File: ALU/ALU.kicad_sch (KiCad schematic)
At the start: 1 part

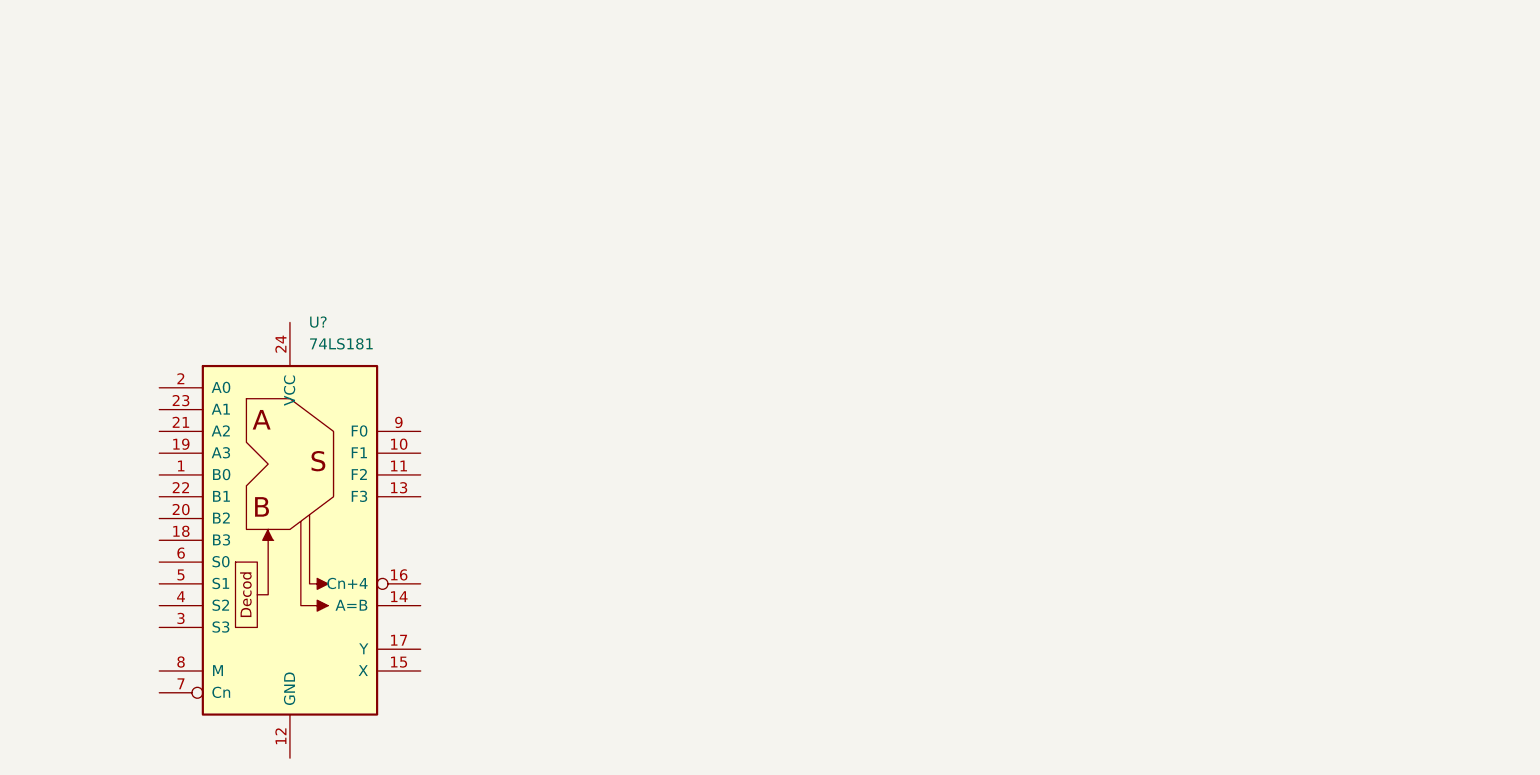
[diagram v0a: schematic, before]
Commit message: Completed ALU first draft
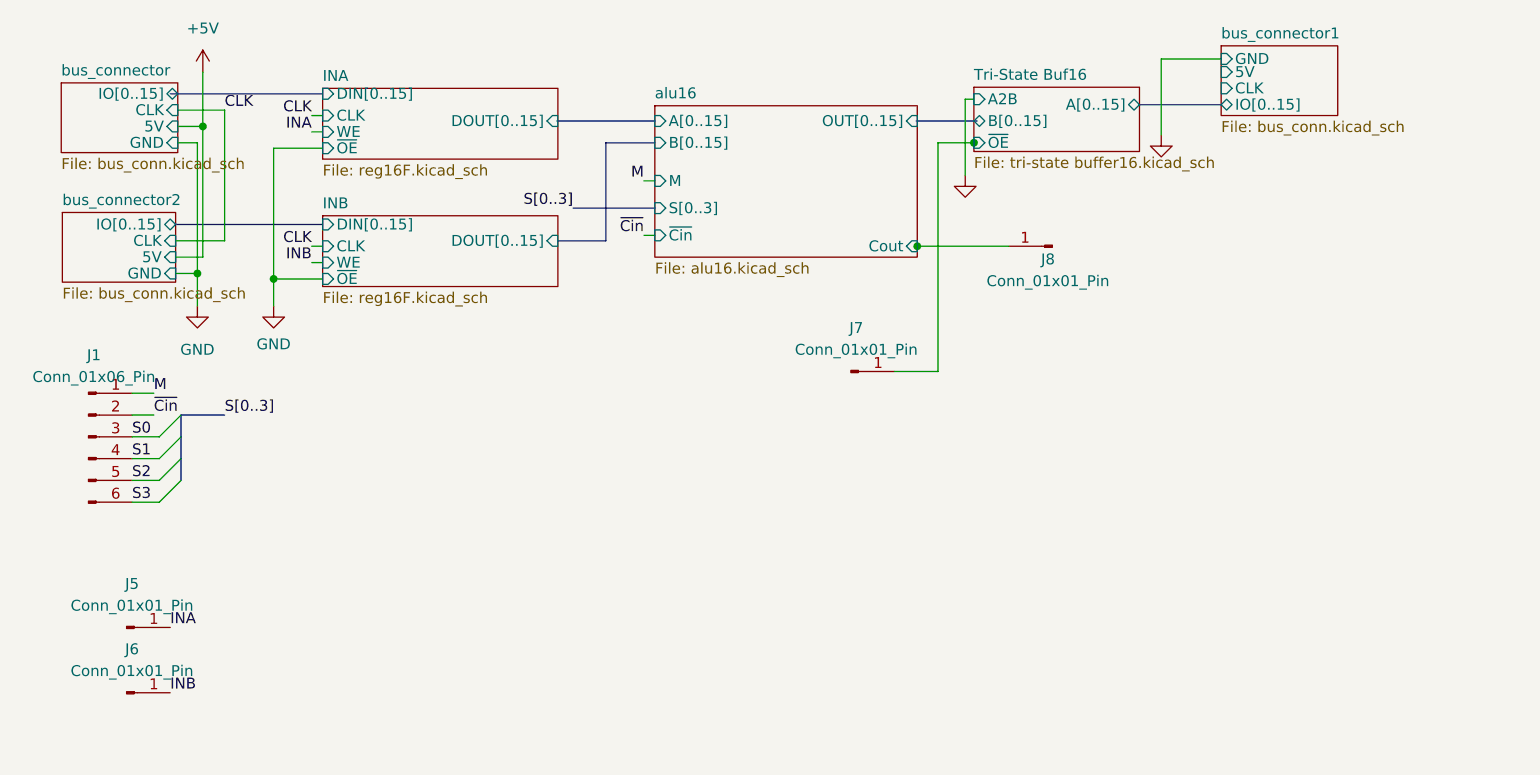
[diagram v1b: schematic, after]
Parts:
- removed U?: 74LS181, symbol 74xx:74LS181
- added J1: Conn_01x06_Pin, Connector_PinHeader_2.54mm:PinHeader_1x06_P2.54mm_Vertical, symbol Connector:Conn_01x06_Pin
- added J5, J6, J7, J8: Conn_01x01_Pin, Connector_PinHeader_2.54mm:PinHeader_1x01_P2.54mm_Vertical, symbol Connector:Conn_01x01_Pin
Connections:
- new net INA: J5.1 (Pin_1)
- new net INB: J6.1 (Pin_1)
- new net M: J1.1 (Pin_1)
- new net S0: J1.3 (Pin_3)
- new net S1: J1.4 (Pin_4)
- new net S2: J1.5 (Pin_5)
- new net S3: J1.6 (Pin_6)
- new net Tri-State Buf16/~{OE}: J7.1 (Pin_1)
- new net alu16/Cout: J8.1 (Pin_1)
- new net ~{Cin}: J1.2 (Pin_2)
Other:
- added sheet INA (reg16F.kicad_sch)
- added sheet INB (reg16F.kicad_sch)
- added sheet Tri-State Buf16 (tri-state buffer16.kicad_sch)
- added sheet alu16 (alu16.kicad_sch)
- added sheet bus_connector (bus_conn.kicad_sch)
- added sheet bus_connector1 (bus_conn.kicad_sch)
- added sheet bus_connector2 (bus_conn.kicad_sch)
- title: (none) -> AOS16 Arithmetic Logic Unit

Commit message: Updated ALU and moved common schematics to common/ for enhanced reusability
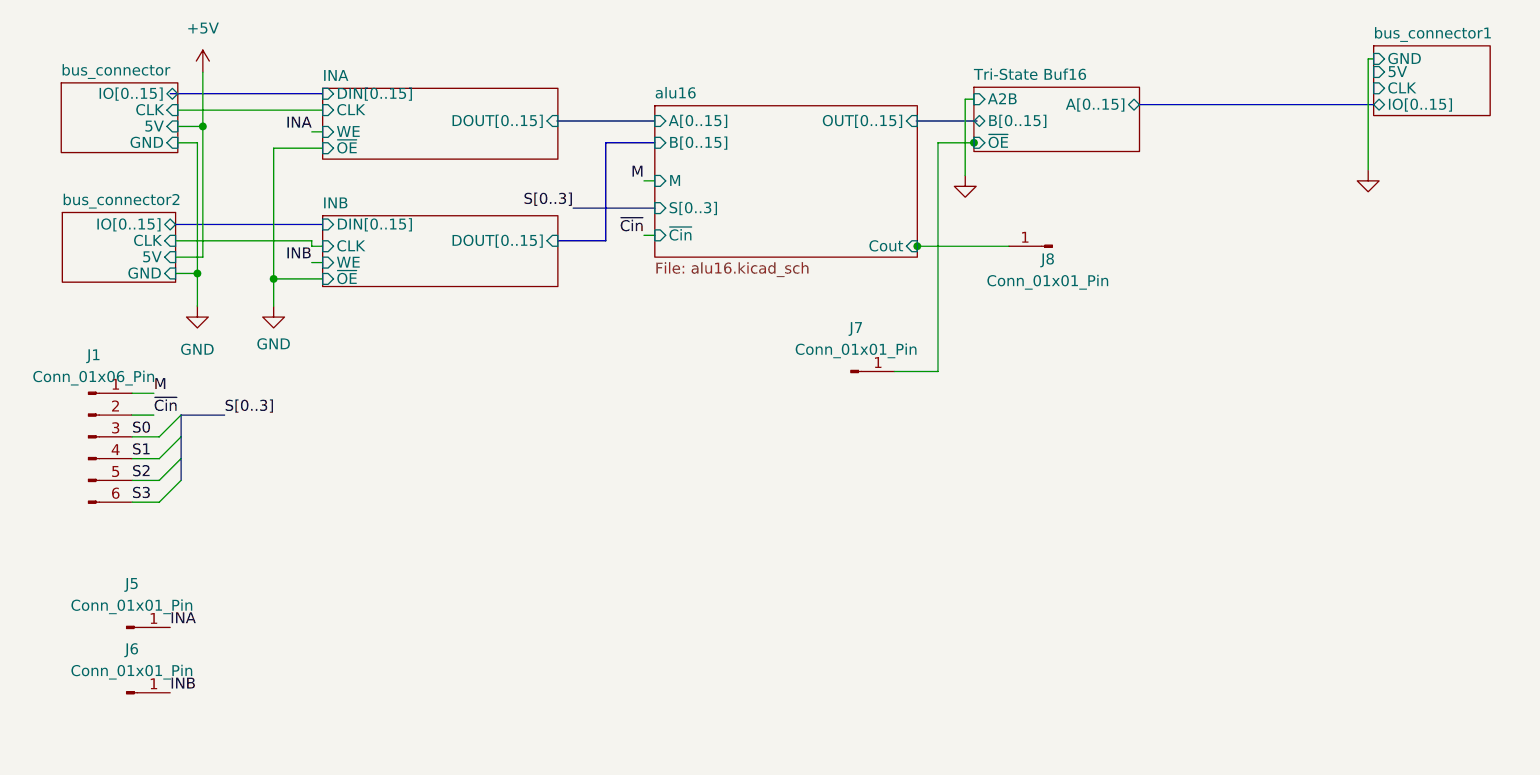
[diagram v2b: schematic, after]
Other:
- sheet INA: file reg16F.kicad_sch -> ../common/reg16F.kicad_sch
- sheet INB: file reg16F.kicad_sch -> ../common/reg16F.kicad_sch
- sheet Tri-State Buf16: file tri-state buffer16.kicad_sch -> ../common/tri-state buffer16.kicad_sch
- sheet bus_connector: file bus_conn.kicad_sch -> ../common/bus_conn.kicad_sch
- sheet bus_connector1: file bus_conn.kicad_sch -> ../common/bus_conn.kicad_sch
- sheet bus_connector2: file bus_conn.kicad_sch -> ../common/bus_conn.kicad_sch
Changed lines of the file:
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@@
 	(wire
 		(pts
-			(xy 31.115 43.815) (xy 36.83 43.815)
+			(xy 31.115 43.815) (xy 46.99 43.815)
 		)
 		(stroke
@@
 	(wire
 		(pts
-			(xy 153.035 22.606) (xy 146.05 22.606)
+			(xy 170.815 22.606) (xy 170.18 22.606)
 		)
 		(stroke
@@
 	(wire
 		(pts
-			(xy 46.99 29.21) (xy 48.26 29.21)
-		)
-		(stroke
-			(width 0)
-			(type default)
-		)
-	)
-	(wire
-		(pts
 			(xy 48.26 33.02) (xy 42.545 33.02)
 		)
@@
 	(wire
 		(pts
-			(xy 146.05 22.606) (xy 146.05 31.496)
+			(xy 170.18 22.606) (xy 170.18 35.56)
 		)
 		(stroke
@@
 	(wire
 		(pts
-			(xy 31.369 28.575) (xy 36.83 28.575)
+			(xy 31.369 28.575) (xy 48.26 28.575)
 		)
 		(stroke
@@
 	(wire
 		(pts
-			(xy 36.83 43.815) (xy 36.83 28.575)
-		)
-		(stroke
-			(width 0)
-			(type default)
-		)
-	)
-	(wire
-		(pts
 			(xy 26.035 69.215) (xy 29.21 69.215)
 		)
@@
 		)
 	)
+	(wire
+		(pts
+			(xy 46.99 43.815) (xy 46.99 44.45)
+		)
+		(stroke
+			(width 0)
+			(type default)
+		)
+	)
 	(bus
 		(pts
-			(xy 143.51 27.94) (xy 153.035 27.94)
+			(xy 143.51 27.94) (xy 170.815 27.94)
 		)
 		(stroke
@@
 		)
 	)
-	(label "CLK"
-		(at 46.99 29.21 180)
+	(label "S1"
+		(at 26.035 69.215 0)
 		(fields_autoplaced yes)
 		(effects
@@
 				(size 1.27 1.27)
 			)
-			(justify right bottom)
-		)
-	)
-	(label "S1"
-		(at 26.035 69.215 0)
+			(justify left bottom)
+		)
+	)
+	(label "S[0..3]"
+		(at 36.83 64.135 0)
 		(fields_autoplaced yes)
 		(effects
@@
 		)
 	)
-	(label "CLK"
-		(at 46.99 44.45 180)
+	(label "INA"
+		(at 30.48 88.9 0)
 		(fields_autoplaced yes)
 		(effects
@@
 				(size 1.27 1.27)
 			)
-			(justify right bottom)
-		)
-	)
-	(label "S[0..3]"
-		(at 36.83 64.135 0)
+			(justify left bottom)
+		)
+	)
+	(label "INB"
+		(at 30.48 96.52 0)
 		(fields_autoplaced yes)
 		(effects
@@
 		)
 	)
-	(label "INA"
-		(at 30.48 88.9 0)
+	(label "M"
+		(at 28.575 61.595 0)
 		(fields_autoplaced yes)
 		(effects
@@
 		)
 	)
-	(label "INB"
-		(at 30.48 96.52 0)
+	(label "S[0..3]"
+		(at 77.47 40.005 180)
 		(fields_autoplaced yes)
 		(effects
@@
 				(size 1.27 1.27)
 			)
-			(justify left bottom)
-		)
-	)
-	(label "M"
-		(at 28.575 61.595 0)
+			(justify right bottom)
+		)
+	)
+	(label "INA"
+		(at 46.99 31.115 180)
 		(fields_autoplaced yes)
 		(effects
@@
 				(size 1.27 1.27)
 			)
-			(justify left bottom)
-		)
-	)
-	(label "S[0..3]"
-		(at 77.47 40.005 180)
+			(justify right bottom)
+		)
+	)
+	(label "S2"
+		(at 26.035 71.755 0)
 		(fields_autoplaced yes)
 		(effects
@@
 				(size 1.27 1.27)
 			)
-			(justify right bottom)
-		)
-	)
-	(label "CLK"
-		(at 36.83 28.575 0)
-		(fields_autoplaced yes)
-		(effects
-			(font
-				(size 1.27 1.27)
-			)
-			(justify left bottom)
-		)
-	)
-	(label "INA"
-		(at 46.99 31.115 180)
-		(fields_autoplaced yes)
-		(effects
-			(font
-				(size 1.27 1.27)
-			)
-			(justify right bottom)
-		)
-	)
-	(label "S2"
-		(at 26.035 71.755 0)
-		(fields_autoplaced yes)
-		(effects
-			(font
-				(size 1.27 1.27)
-			)
 			(justify left bottom)
 		)
@@
 	(symbol
 		(lib_id "power:GND")
-		(at 146.05 31.496 0)
+		(at 170.18 35.56 0)
 		(unit 1)
 		(exclude_from_sim no)
@@
 		(fields_autoplaced yes)
 		(property "Reference" "#PWR05"
-			(at 146.05 37.846 0)
+			(at 170.18 41.91 0)
 			(effects
 				(font
@@
 		)
 		(property "Value" "GND"
-			(at 146.05 35.941 0)
+			(at 170.18 40.005 0)
 			(effects
 				(font
@@
 		)
 		(property "Footprint" ""
-			(at 146.05 31.496 0)
+			(at 170.18 35.56 0)
 			(effects
 				(font
@@
 		)
 		(property "Datasheet" ""
-			(at 146.05 31.496 0)
+			(at 170.18 35.56 0)
 			(effects
 				(font
@@
 		)
 		(property "Description" "Power symbol creates a global label with name \"GND\" , ground"
-			(at 146.05 31.496 0)
+			(at 170.18 35.56 0)
 			(effects
 				(font
@@
 			)
 		)
-		(property "Sheetfile" "tri-state buffer16.kicad_sch"
+		(property "Sheetfile" "../common/tri-state buffer16.kicad_sch"
 			(at 124.206 33.9856 0)
 			(effects
@@
 				)
 				(justify left top)
+				(hide yes)
 			)
 		)
@@
 			)
 		)
-		(property "Sheetfile" "bus_conn.kicad_sch"
+		(property "Sheetfile" "../common/bus_conn.kicad_sch"
 			(at 17.907 49.2256 0)
 			(effects
@@
 				)
 				(justify left top)
+				(hide yes)
 			)
 		)
@@
 		(at 17.78 25.4)
 		(size 13.589 8.128)
-		(fields_autoplaced yes)
 		(stroke
 			(width 0.1524)
@@
 			)
 		)
-		(property "Sheetfile" "bus_conn.kicad_sch"
-			(at 17.78 34.1126 0)
+		(property "Sheetfile" "../common/bus_conn.kicad_sch"
+			(at 12.954 34.798 0)
 			(effects
 				(font
@@
 				)
 				(justify left top)
+				(hide yes)
 			)
 		)
@@
 	)
 	(sheet
-		(at 153.035 21.082)
+		(at 170.815 21.082)
 		(size 13.589 8.128)
 		(fields_autoplaced yes)
@@
 		)
 		(property "Sheetname" "bus_connector1"
-			(at 153.035 20.3704 0)
+			(at 170.815 20.3704 0)
 			(effects
 				(font
@@
 			)
 		)
-		(property "Sheetfile" "bus_conn.kicad_sch"
-			(at 153.035 29.7946 0)
+		(property "Sheetfile" "../common/bus_conn.kicad_sch"
+			(at 170.815 29.7946 0)
 			(effects
 				(font
@@
 				)
 				(justify left top)
+				(hide yes)
 			)
 		)
 		(pin "5V" input
-			(at 153.035 24.13 180)
+			(at 170.815 24.13 180)
 			(effects
 				(font
@@
 		)
 		(pin "GND" input
-			(at 153.035 22.606 180)
+			(at 170.815 22.606 180)
 			(effects
 				(font
@@
 		)
 		(pin "IO[0..15]" tri_state
-			(at 153.035 27.94 180)
+			(at 170.815 27.94 180)
 			(effects
 				(font
@@
 		)
 		(pin "CLK" input
-			(at 153.035 26.035 180)
+			(at 170.815 26.035 180)
 			(effects
 				(font
@@
 			)
 		)
-		(property "Sheetfile" "reg16F.kicad_sch"
+		(property "Sheetfile" "../common/reg16F.kicad_sch"
 			(at 48.26 49.7336 0)
 			(effects
@@
 				)
 				(justify left top)
+				(hide yes)
 			)
 		)
@@
 			)
 		)
-		(property "Sheetfile" "reg16F.kicad_sch"
+		(property "Sheetfile" "../common/reg16F.kicad_sch"
 			(at 48.26 34.8746 0)
 			(effects
@@
 				)
 				(justify left top)
+				(hide yes)
 			)
 		)
@@
 		)
 		(pin "CLK" input
-			(at 48.26 29.21 180)
-			(effects
-				(font
+			(at 48.26 28.575 180)
+			(effects
+				(font

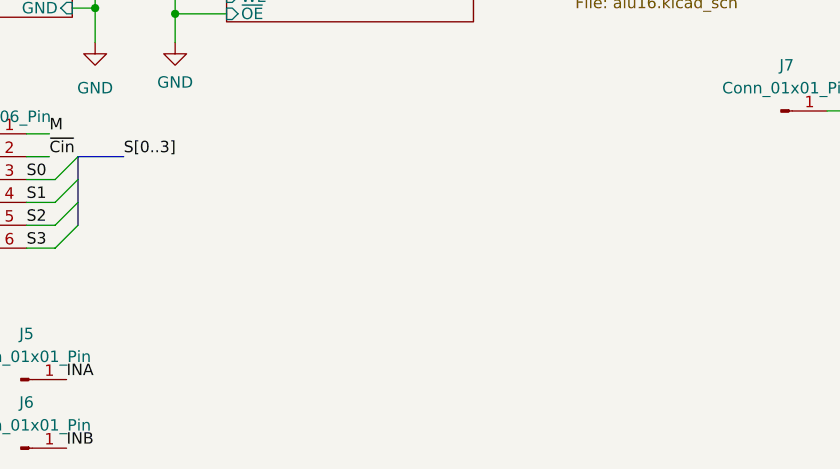
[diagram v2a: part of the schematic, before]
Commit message: Fixed silkscreen on ALU and Double Buffer
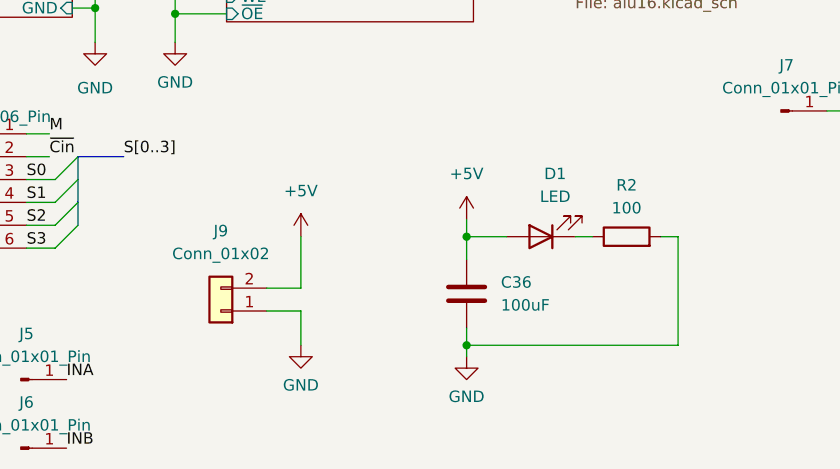
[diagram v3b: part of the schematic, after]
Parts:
- added C36: 100uF, Capacitor_SMD:CP_Elec_5x5.3, symbol Device:C
- added D1: LED, LED_SMD:LED_0603_1608Metric, symbol Device:LED
- added J9: Conn_01x02, Connector_PinHeader_2.54mm:PinHeader_1x02_P2.54mm_Vertical, symbol Connector_Generic:Conn_01x02
- added R2: 100, Resistor_SMD:R_0603_1608Metric, symbol Device:R
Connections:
- net +5V: now also C36.1, D1.2 (A), J9.2 (Pin_2)
- net GND: now also C36.2, J9.1 (Pin_1), R2.2
- new net: D1.1 (K), R2.1

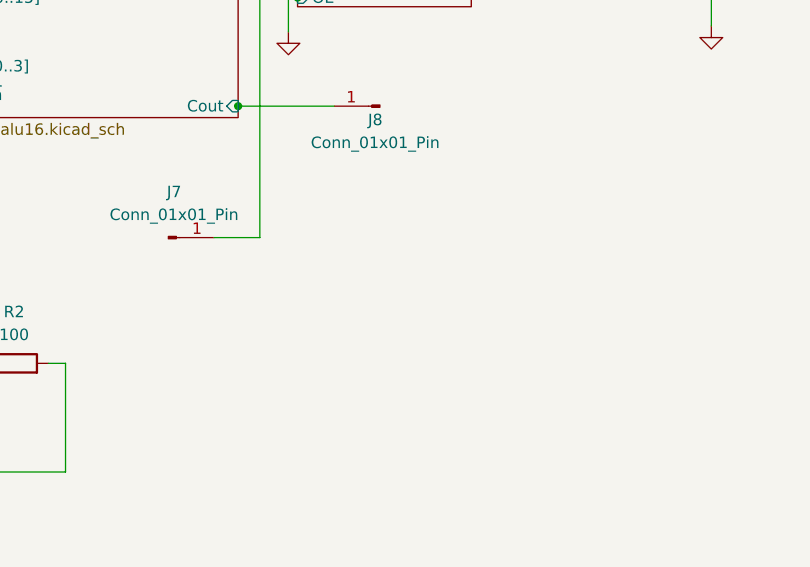
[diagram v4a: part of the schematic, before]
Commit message: Fixed register data flow direction and added mounitng holes to ALU
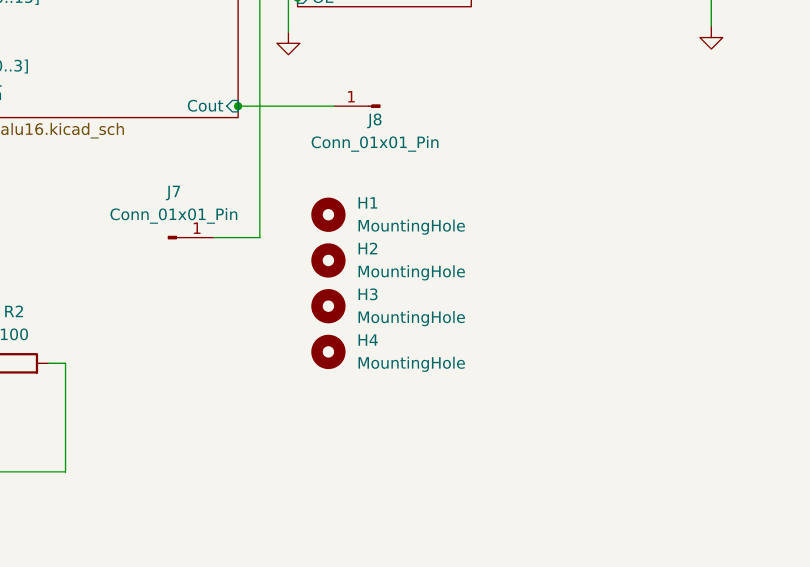
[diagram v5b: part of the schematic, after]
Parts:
- added H1, H2, H3, H4: MountingHole, MountingHole:MountingHole_4mm, symbol Mechanical:MountingHole

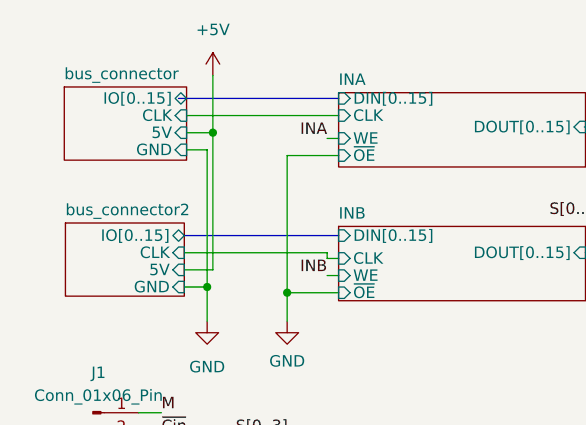
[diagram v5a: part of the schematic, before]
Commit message: Memory Controller fabrication checks complete
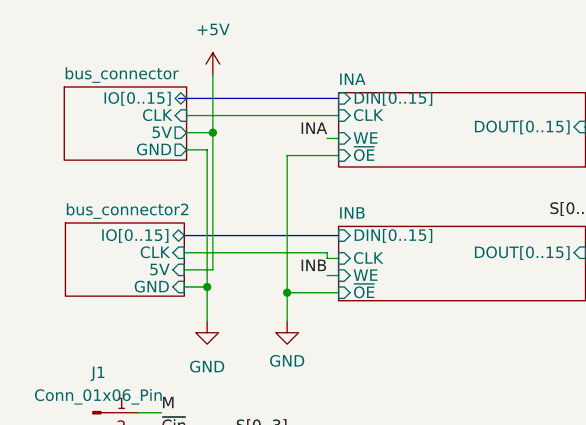
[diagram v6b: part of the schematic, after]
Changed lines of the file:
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@@
 			)
 		)
-		(pin "5V" input
+		(pin "5V" output
 			(at 31.369 30.48 0)
 			(effects
@@
 			)
 		)
-		(pin "GND" input
+		(pin "GND" output
 			(at 31.369 32.385 0)
 			(effects
